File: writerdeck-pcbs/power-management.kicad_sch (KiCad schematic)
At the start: 36 parts, among them J1 5000mAh 3.7V LiPo, J3 5000mAh 3.7V LiPo, U2 BQ25792RQMR

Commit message: power management done
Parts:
- removed C10, C11, C15, C16, C17, C18, C19, C23, C24, C5, C6, C9: 10u, symbol Device:C
- removed C12, C13: 47n, symbol Device:C
- removed C14, C4, C8: 0.1u, symbol Device:C
- removed C20: 1n, symbol Device:C
- removed C3: 4.7u, symbol Device:C
- removed C7: 2.2u, symbol Device:C
- removed D1: LED, symbol Device:LED
- removed J1, J3: 5000mAh 3.7V LiPo, symbol Connector_Generic:Conn_01x02
- removed L1: 10u, symbol Device:L
- removed R1: 2, symbol Device:R
- removed R10, R9: 10k, symbol Device:R
- removed R12: 100, symbol Device:R
- removed R3: 6.04k, symbol Device:R
- removed R4, R5: R, symbol Device:R
- removed R6: 2.2k, symbol Device:R
- removed R7: 5.24k, symbol Device:R
- removed R8: 30.31k, symbol Device:R
- removed TH2: 10k, symbol Device:Thermistor_NTC
- added C1, C10, C11, C15, C16, C17, C18, C19, C20, C23, C5, C6, C9: 10u, Capacitor_SMD:C_0603_1608Metric, symbol ZF_common:10u 10% 0603 Capacitor
- added C12, C13: 47n, Capacitor_SMD:C_0603_1608Metric, symbol ZF_common:47n 5% 0603 Capacitor
- added C14, C4, C8: 100n, Capacitor_SMD:C_0603_1608Metric, symbol ZF_common:100n 5% 0603 Capacitor
- added C2, C24, C25: 22u, Capacitor_SMD:C_0603_1608Metric, symbol ZF_common:22u 10% 0603 Capacitor
- added C3: 4u7, Capacitor_SMD:C_0603_1608Metric, symbol ZF_common:4u7 10% 0603 Capacitor
- added C7: 2u2, Capacitor_SMD:C_0603_1608Metric, symbol ZF_common:2u2 10% 0603 Capacitor
- added D1: Blue LED, LED_SMD:LED_0805_2012Metric, symbol ZF_common:0805 Blue LED
- added J1, J2: 5023520300, ZF_common:5023520300, symbol ZF_common:5023520300
- added L2: 1u, ZF_common:XFL4020-102MEC, symbol ZF_common:1uH XFL4020-102MEC
- added Q1: CSD17575Q3, Package_TO_SOT_SMD:TDSON-8-1, symbol Transistor_FET:CSD17570Q5B
- added R1: 2, Resistor_SMD:R_0603_1608Metric, symbol ZF_common:2 1% 0603 Resistor
- added R10, R13, R17, R2, R4, R9: 10k, Resistor_SMD:R_0603_1608Metric, symbol ZF_common:10k 1% 0603 Resistor
- added R12, R25: 100, Resistor_SMD:R_0603_1608Metric, symbol ZF_common:100 0.1% 0603 Resistor
- added R14, R18: 100k, Resistor_SMD:R_0603_1608Metric, symbol ZF_common:100k 1% 0603 Resistor
- added R19: 732k, Resistor_SMD:R_0603_1608Metric, symbol ZF_common:732k 1% 0603 Resistor
- added R20: 620, Resistor_SMD:R_0603_1608Metric, symbol ZF_common:620 1% 0603 Resistor
- added R24: 15k, Resistor_SMD:R_0603_1608Metric, symbol ZF_common:15k 1% 0603 Resistor
- added R26: 50, Resistor_SMD:R_0603_1608Metric, symbol ZF_common:50 0.1% 0603 Resistor
- added R3: 3k, Resistor_SMD:R_0603_1608Metric, symbol ZF_common:3k 1% 0603 Resistor
- added R5: 300k, Resistor_SMD:R_0603_1608Metric, symbol ZF_common:300k 1% 0603 Resistor
- added R6: 2k2, Resistor_SMD:R_0603_1608Metric, symbol ZF_common:2k2 1% 0603 Resistor
- added R8: 2k, Resistor_SMD:R_0603_1608Metric, symbol ZF_common:2k 1% 0603 Resistor
- added SW1: PWR BUT, symbol Switch:SW_Push
- added U4: TPS61022, Package_DFN_QFN:Texas_RWU0007A_VQFN-7_2x2mm_P0.5mm, symbol Converter_DCDC:TPS61022
- U2: DKN 296-BQ25792RQMRCT-ND -> (none); LCSCN (none) -> C2862876; MFR (none) -> Texas Instruments
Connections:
- net BATP: now also R12.2
- net BTST1: now also C13.1
- net BTST2: now also C12.2
- net GND: now also C1.2, C10.2, C11.2, C14.2, C15.2, C16.2, C17.2, C18.2, C19.2, C2.2, C20.2, C23.2, C24.2, C25.2, C3.2, C4.2, C5.2, C6.2, C7.2, C8.2, C9.2, J1.3 (Pin_3), J2.3 (Pin_3), R18.2, R2.1, R26.2, R3.2, R5.2, SW1.2, U4.1 (GND)
- net ILIM_HIZ: now also R14.2, R5.1
- net INT: now also R13.1; no longer U2.21 (~{INT})
- net REGN: now also C3.1, R14.1, R4.1, R6.1, R8.1
- net SCL: now also R9.1
- net SDA: now also R10.2
- net STAT: now also D1.1 (K)
- net SW1: now also C13.2
- net SW2: now also C12.1
- net VBUS: now also C4.1, C5.1, C6.1, R1.1
- net V_BATT: now also J1.1 (Pin_1), J2.1 (Pin_1), Q1.1 (S), Q1.2 (S), Q1.3 (S), R12.1; no longer U2.22 (BAT), U2.23 (BAT__1)
- net at U2.14 (SCL): now also R9.2
- net at U2.15 (SDA): now also R10.1
- net SDRV: now reaches U2.24 (SDRV)
- net SDRV: now also Q1.4 (G)
- net CE: no longer names the net of U2.13 (~{CE})
- net CE: now also R2.2
- net PMID: no longer names the net of U2.29 (PMID)
- net PMID: now also C10.1, C11.1, C8.1, C9.1
- net PROG: no longer names the net of U2.20 (PROG)
- net PROG: now also R3.1
- net QON renamed PWR_BUT
- net PWR_BUT: now also R4.2, SW1.1
- net SYS renamed VSYS
- net VSYS: now also C1.1, C14.1, C15.1, C16.1, C17.1, C18.1, C19.1, L2.1, R17.1, U4.7 (VIN)
- net TS renamed BATT_TEMP
- net BATT_TEMP: now also J1.2 (Pin_2), J2.2 (Pin_2), R20.2, R24.1
- new net: D1.2 (A), R6.2
- new net: R25.2, R26.1
- new net: R13.2, U2.21 (~{INT})
- new net: L2.2, U4.2 (SW)
- new net: R18.1, R19.2, U4.4 (FB)
- new net: R17.2, U4.5 (EN), U4.6 (MODE)
- new net: R20.1, R8.2
- new net: R24.2, R25.1
- new net: C7.1, R1.2
- new net +5V: C2.1, C24.1, C25.1, R19.1, U4.3 (VOUT)
- new net BAT: C20.1, C23.1, Q1.5 (D), U2.22 (BAT), U2.23 (BAT__1)
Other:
- note removed: "NEED PROGRAM"
- note removed: "SYSTEM LOAD"
- moved on the sheet: U2

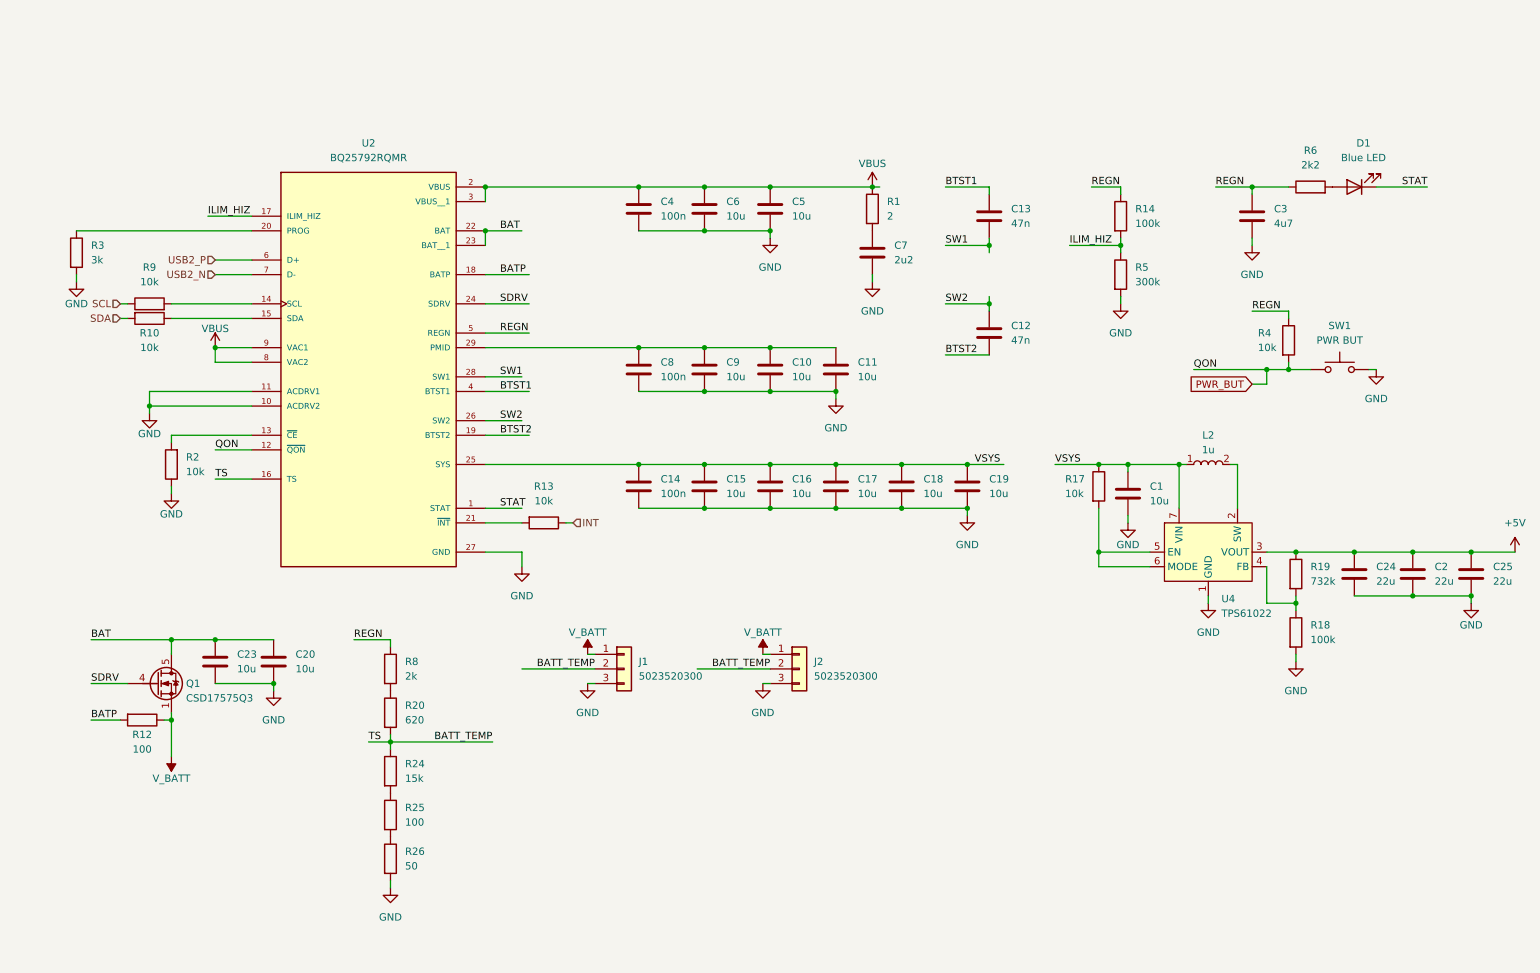
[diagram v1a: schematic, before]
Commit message: pre switch matrix, restructure
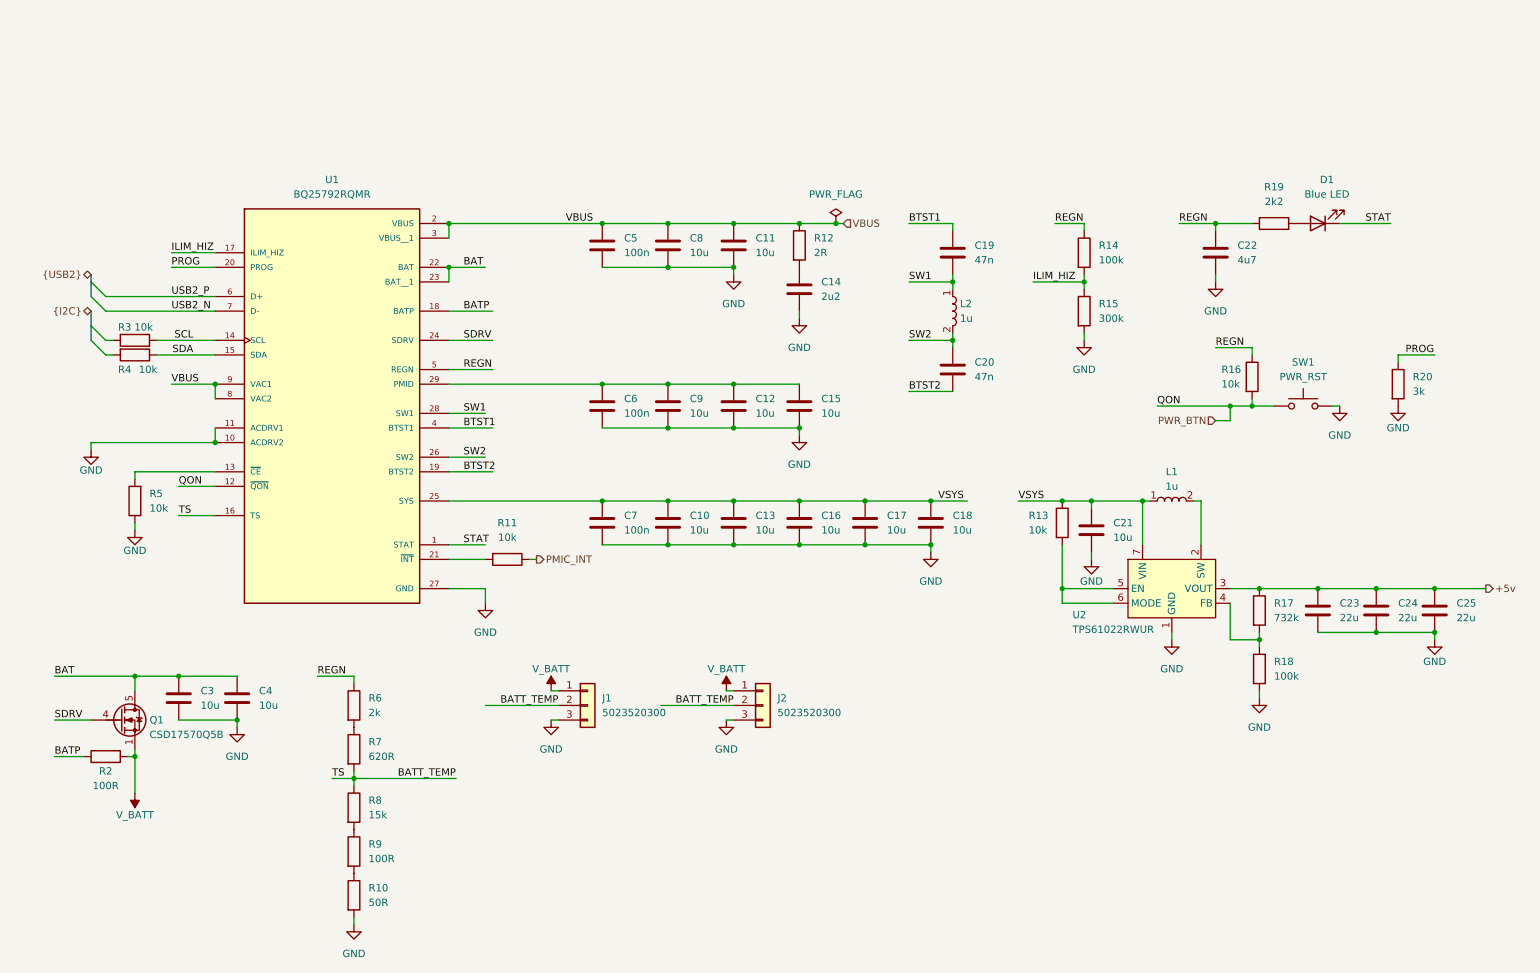
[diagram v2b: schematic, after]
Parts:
- removed R1: 2, Resistor_SMD:R_0603_1608Metric, symbol ZF_common:2 1% 0603 Resistor
- removed R12, R25: 100, Resistor_SMD:R_0603_1608Metric, symbol ZF_common:100 0.1% 0603 Resistor
- removed R20: 620, Resistor_SMD:R_0603_1608Metric, symbol ZF_common:620 1% 0603 Resistor
- removed R26: 50, Resistor_SMD:R_0603_1608Metric, symbol ZF_common:50 0.1% 0603 Resistor
- removed U4: TPS61022, Package_DFN_QFN:Texas_RWU0007A_VQFN-7_2x2mm_P0.5mm, symbol Converter_DCDC:TPS61022
- added L2: 1u, ZF_common:XFL4020-102MEC, symbol ZF_common:1uH XFL4020-102MEC
- added R10: 50R, Resistor_SMD:R_0603_1608Metric, symbol ZF_common:50R 0.1% 0603 Resistor
- added R12: 2R, Resistor_SMD:R_0603_1608Metric, symbol ZF_common:2R 1% 0603 Resistor
- added R2, R9: 100R, Resistor_SMD:R_0603_1608Metric, symbol ZF_common:100R 0.1% 0603 Resistor
- added R7: 620R, Resistor_SMD:R_0603_1608Metric, symbol ZF_common:620R 1% 0603 Resistor
- added U2: TPS61022RWUR, Package_DFN_QFN:Texas_RWU0007A_VQFN-7_2x2mm_P0.5mm, symbol ZF_common:TPS61022
- Q1: value CSD17575Q3 -> CSD17570Q5B
- SW1: value PWR BUT -> PWR_RST
- renumbered C15 to C10, C5 to C11, C10 to C12, C16 to C13, C7 to C14, C11 to C15, C17 to C16, C18 to C17, C19 to C18, C13 to C19, C12 to C20, C1 to C21, C3 to C22, C24 to C23, C2 to C24, C23 to C3, C20 to C4, C4 to C5, C8 to C6, C14 to C7, C6 to C8, L2 to L1, R13 to R11, R17 to R13, R5 to R15, R4 to R16, R19 to R17, R6 to R19, R3 to R20, R9 to R3, R10 to R4, R2 to R5, R8 to R6, R24 to R8, U2 to U1
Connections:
- net BATP: now also R2.1
- net BATT_TEMP: now also R7.2
- net GND: now also R10.2, U2.1 (GND)
- net SCL: now also R3.2, U1.14 (SCL); no longer R3.1
- net SDA: now also R4.1, U1.15 (SDA); no longer R4.2
- net SW1: now also L2.1
- net SW2: now also L2.2
- net VBUS: now also R12.1
- net VSYS: now also U2.7 (VIN)
- net V_BATT: now also R2.2
- net at L1.2: now also U2.2 (SW)
- net at R17.2, R18.1: now also U2.4 (FB)
- net at R13.2: now also U2.5 (EN), U2.6 (MODE)
- net PROG: now reaches R20.1, U1.20 (PROG)
- net at R6.2: now also R7.1
- net at R8.2: now also R9.1
- net at C14.1: now also R12.2
- net +5V renamed +5v
- net +5v: now also U2.3 (VOUT)
- net INT renamed PMIC_INT
- net PWR_BUT renamed PWR_BTN
- new net: R10.1, R9.2
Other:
- moved on the sheet: C10, C11, C12, C13, C14, C15, C16, C17, C18, C19, C20, C21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

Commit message: backup
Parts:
- removed SW1: PWR_RST, symbol Switch:SW_Push
- added SW1: Tact Switch, symbol ZF_common:Tact Switch
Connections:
- net GND: now also SW1.3 (K), SW1.4 (A)
- net PWR_BTN: now also SW1.1, SW1.2
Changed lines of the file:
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@@
 	)
 	(junction
+		(at 243.84 83.82)
+		(diameter 0)
+		(color 0 0 0 0)
+	)
+	(junction
 		(at 151.13 107.95)
 		(diameter 0)
@@
 	)
 	(junction
+		(at 233.68 83.82)
+		(diameter 0)
+		(color 0 0 0 0)
+	)
+	(junction
 		(at 151.13 52.07)
 		(diameter 0)
@@
 	(wire
 		(pts
+			(xy 233.68 81.28) (xy 233.68 83.82)
+		)
+		(stroke
+			(width 0)
+			(type default)
+		)
+	)
+	(wire
+		(pts
 			(xy 39.37 74.93) (xy 49.53 74.93)
 		)
@@
 	(wire
 		(pts
+			(xy 243.84 81.28) (xy 243.84 83.82)
+		)
+		(stroke
+			(width 0)
+			(type default)
+		)
+	)
+	(wire
+		(pts
 			(xy 35.56 143.51) (xy 35.56 144.78)
 		)
@@
 	)
 	(symbol
-		(lib_id "Switch:SW_Push")
-		(at 238.76 83.82 0)
-		(unit 1)
-		(exclude_from_sim no)
-		(in_bom yes)
-		(on_board yes)
-		(dnp no)
-		(fields_autoplaced yes)
-		(property "Reference" "SW1"
-			(at 238.76 76.2 0)
-			(effects
-				(font
-					(size 1.27 1.27)
-				)
-			)
-		)
-		(property "Value" "PWR_RST"
-			(at 238.76 78.74 0)
-			(effects
-				(font
-					(size 1.27 1.27)
-				)
-			)
-		)
-		(property "Footprint" ""
-			(at 238.76 78.74 0)
-			(effects
-				(font
-					(size 1.27 1.27)
-				)
-				(hide yes)
-			)
-		)
-		(property "Datasheet" "~"
-			(at 238.76 78.74 0)
-			(effects
-				(font
-					(size 1.27 1.27)
-				)
-				(hide yes)
-			)
-		)
-		(property "Description" "Push button switch, generic, two pins"
-			(at 238.76 83.82 0)
-			(effects
-				(font
-					(size 1.27 1.27)
-				)
-				(hide yes)
-			)
-		)
-		(pin "2"
-		)
-		(pin "1"
-		)
-		(instances
-			(project "writerdeck-pcbs"
-				(path "/61242ec3-a4bb-4627-ba23-da2822f5a571/941d0643-0a3b-4b04-bc4b-d64fb2409d8b"
-					(reference "SW1")
-					(unit 1)
-				)
-			)
-		)
-	)
-	(symbol
 		(lib_id "ZF_common:300k 1% 0603 Resistor")
 		(at 200.66 67.31 0)
@@
 					(unit 1)
 				)
+			)
+		)
+	)
+	(symbol
+		(lib_id "ZF_common:Tact Switch")
+		(at 238.76 83.82 0)
+		(unit 1)
+		(exclude_from_sim no)
+		(in_bom yes)
+		(on_board yes)
+		(dnp no)
+		(fields_autoplaced yes)
+		(property "Reference" "SW1"
+			(at 238.76 73.66 0)
+			(effects
+				(font
+					(size 1.27 1.27)
+				)
+			)
+		)
+		(property "Value" "Tact Switch"
+			(at 238.76 76.2 0)
+			(effects
+				(font
+					(size 1.27 1.27)
+				)
+			)
+		)
+		(property "Footprint" ""
+			(at 238.76 76.2 0)
+			(effects
+				(font
+					(size 1.27 1.27)
+				)
+				(hide yes)
+			)
+		)
+		(property "Datasheet" ""
+			(at 238.76 76.2 0)
+			(effects
+				(font
+					(size 1.27 1.27)
+				)
+				(hide yes)
+			)
+		)
+		(property "Description" "temp"
+			(at 238.76 83.82 0)
+			(effects
+				(font
+					(size 1.27 1.27)
+				)
+				(hide yes)
+			)
+		)
+		(pin "3"
+		)
+		(pin "2"
+		)
+		(pin "4"
+		)
+		(pin "1"
+		)
+		(instances
+			(project ""
+				(path "/61242ec3-a4bb-4627-ba23-da2822f5a571/941d0643-0a3b-4b04-bc4b-d64fb2409d8b"
+					(reference "SW1")
+					(unit 1)
+				)
